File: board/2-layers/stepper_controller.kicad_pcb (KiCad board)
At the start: 4 copper layers, 99 x 46 mm, 51 parts, among them J201 USB_OTG, P103 M3_AOUT, P104 M3_BOUT, P105 M2_AOUT, P106 M2_BOUT, P107 M1_AOUT, P108 M1_BOUT, P201 UART1, P301 12V_Conn, U101 DRV8825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

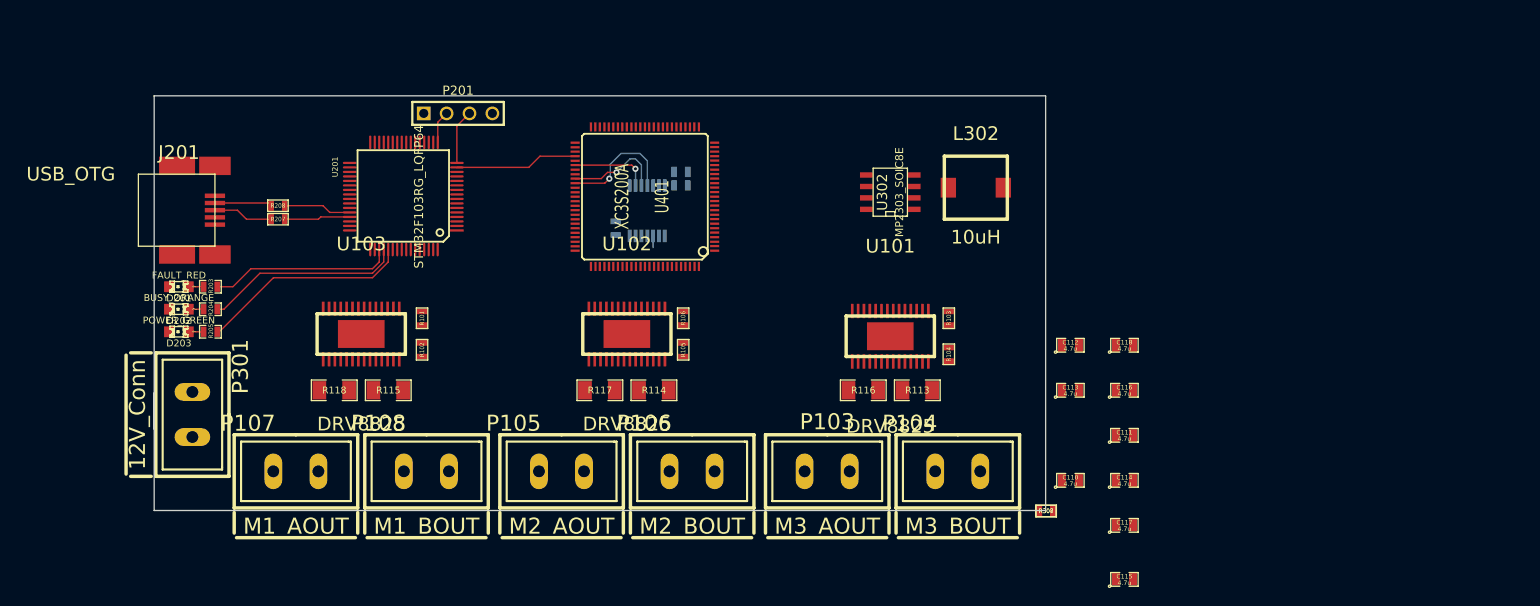
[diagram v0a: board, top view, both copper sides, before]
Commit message: routing first driver
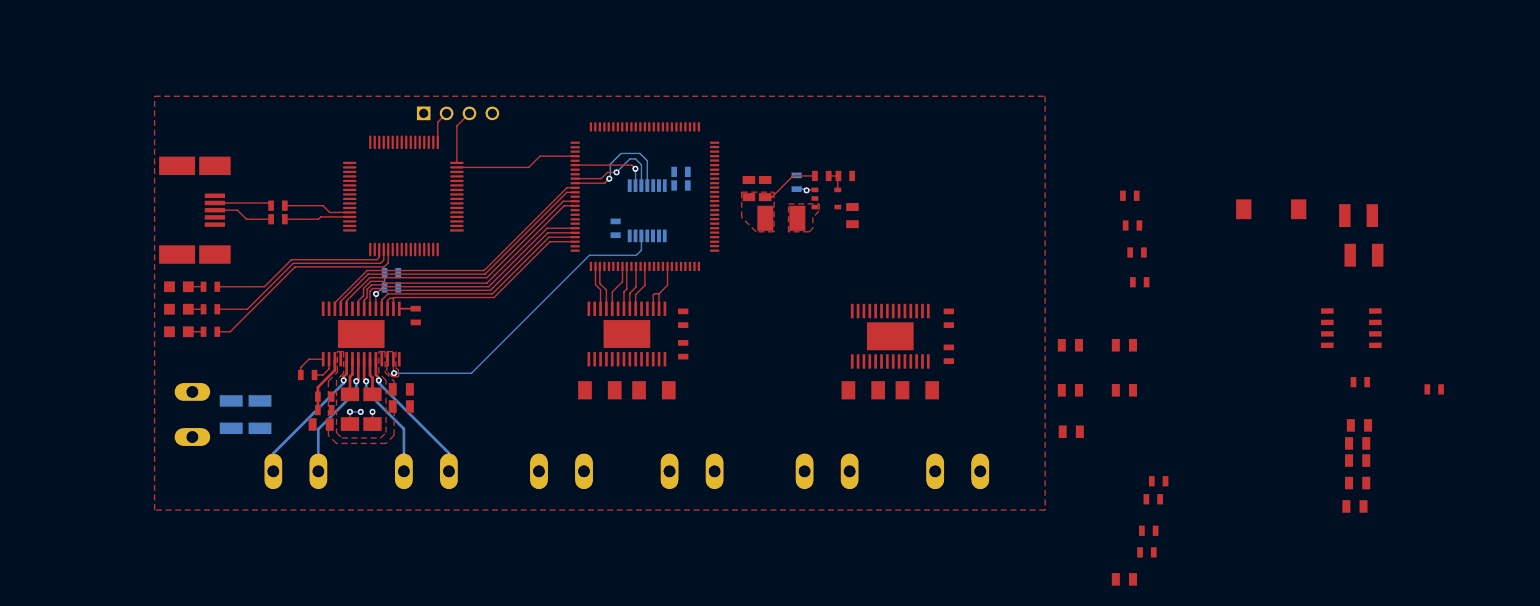
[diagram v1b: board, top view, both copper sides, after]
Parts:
- added C103: 0.47u, SM0603, F.Cu at (134.3, 110.7)
- added C106: 0.1u, SM0603, F.Cu at (124.2, 119.7)
- added C107: 10n, SM0603, F.Cu at (213.9, 100.7)
- added C108: 10n, SM0603, F.Cu at (214.4, 103.7)
- added C109: 10n, SM0603, F.Cu at (122.3, 117.3)
- added C301: 4.7u, SM0805, F.Cu at (182.8, 99.6)
- added C302: 4.7u, SM0805, F.Cu at (173.1, 96.6)
- added C303: 4.7u, SM0805, F.Cu at (171.3, 96.6)
- added C304: 10uF, SM1210, F.Cu at (239.0, 99.6)
- added C305: 10uF, SM1210, F.Cu at (239.6, 104.0)
- added C306: 4.7nF, SM0603, F.Cu at (239.2, 118.1)
- added C307: 0.1uF, SM0603, F.Cu at (215.7, 134.6)
- added C308: 10nF, SM0603, F.Cu at (215.5, 137.0)
- added C309: 1uF, SM1210, B.Cu at (117.0, 121.7)
- added C310: 4.7uF, SM1210, B.Cu at (113.8, 121.7)
- added C311: 10uF, SM0805, F.Cu at (239.1, 122.9)
- added C312: 1uF, SM0805, F.Cu at (238.9, 126.8)
- added C313: 10uF, SM0805, F.Cu at (238.9, 124.9)
- added C314: 10uF, SM0805, F.Cu at (238.9, 129.3)
- added C315: 10uF, SM0805, F.Cu at (238.6, 131.9)
- added L301: 1u, SM1210L, F.Cu at (174.9, 99.9)
- added R107: 1M, SM0603, F.Cu at (124.2, 121.2)
- added R301: 10k, SM0603, B.Cu at (176.6, 95.9)
- added R302: 200k, SM0603, F.Cu at (179.4, 95.2)
- added R303: 200k, SM0603, F.Cu at (182.0, 95.2)
- added R304: 100k, SM0603, F.Cu at (216.8, 129.1)
- added R305: 4.42k, SM0603, F.Cu at (247.4, 118.9)
- added R306: 47k, SM0603, F.Cu at (216.2, 131.1)
- added U301: MP2128-SOT23, SOT23-5, F.Cu at (179.9, 97.7)
- R101, R102: moved to B.Cu
- moved C117 89.9 mm to (123.8, 122.8), turned to 180 degrees
- moved C114 80.7 mm to (132.7, 120.8)
- moved C111 80.5 mm to (132.7, 118.9)
- moved U302 53.4 mm to (238.2, 112.1)
- moved R307 36.2 mm to (213.6, 97.4)
- moved L302 32.9 mm to (229.3, 98.9)
- moved R308 27.5 mm to (214.7, 107.0), turned to 180 degrees
- moved R102 9.15 mm to (131.6, 106.0), turned to 180 degrees
- moved C110 5.40 mm to (207.1, 123.6)
- moved R101 4.81 mm to (131.6, 107.6), turned to 0 degrees
- moved R115 2.73 mm to (129.5, 121.1), turned to 270 degrees
- moved R118 2.73 mm to (127.0, 121.1), turned to 270 degrees
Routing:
- net /VRF_0: track 0.00 -> 36.3 mm, vias 0 -> 1
- net /FPGA/M0_MODE2: track 0.00 -> 32.6 mm
- net /FPGA/M0_MODE1: track 0.00 -> 31.9 mm
- net /FPGA/M0_MODE0: track 0.00 -> 30.8 mm
- net /FPGA/M0_STEP: track 0.00 -> 30.0 mm
- net /FPGA/M0_EN: track 0.00 -> 28.4 mm
- net /FPGA/M0_DIR: track 0.00 -> 27.6 mm
- net /FPGA/M0_RESET: track 0.00 -> 25.6 mm
- net /FPGA/M0_FAULT: track 0.00 -> 25.3 mm
- net /MOT_A1_0: track 0.00 -> 15.8 mm, vias 0 -> 1
- net /MOT_B1_0: track 0.00 -> 15.8 mm, vias 0 -> 1
- net /MOT_A2_0: track 0.00 -> 14.3 mm, vias 0 -> 1
- net /MOT_B2_0: track 0.00 -> 14.3 mm, vias 0 -> 1
- net /FPGA/M1_RESET: track 0.00 -> 7.33 mm
- net +1.2V: track 0.00 -> 6.51 mm
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- added copper zone on F.Cu, net +1.2V
- added copper zone on F.Cu, net +12V
- added copper zone on F.Cu, net /VRF_0
- added copper zone on F.Cu, net GND
- added copper zone on F.Cu, net N-00000140
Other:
- board outline removed
- net class 3.3V added: clearance 0.16, trace_width 0.2, via_dia 0.6858, via_drill 0.3302

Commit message: routed 3 drivers
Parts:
- added C101: 0.47u, SM0603, F.Cu at (193.7, 109.9)
- added C102: 0.47u, SM0603, F.Cu at (163.8, 110.8)
- added C104: 0.1u, SM0603, F.Cu at (183.2, 119.7)
- added C105: 0.1u, SM0603, F.Cu at (153.7, 119.7)
- added R108: 1M, SM0603, F.Cu at (153.7, 121.2)
- added R109: 1M, SM0603, F.Cu at (183.2, 121.2)
- R103, R104, R105, R106: moved to B.Cu
- moved C108 64.1 mm to (151.8, 117.3)
- moved C110 53.8 mm to (153.3, 122.9), turned to 180 degrees
- moved C116 50.8 mm to (162.2, 120.8)
- moved C113 44.8 mm to (162.2, 118.9)
- moved C107 36.6 mm to (181.3, 117.3)
- moved R105 10.5 mm to (158.5, 105.5), turned to 0 degrees
- moved R104 9.40 mm to (188.1, 107.3), turned to 0 degrees
- moved R103 7.50 mm to (188.1, 105.8), turned to 180 degrees
- moved R106 6.80 mm to (158.5, 107.0), turned to 180 degrees
- moved R301 5.55 mm to (180.9, 99.3), turned to 90 degrees
- moved C302 4.87 mm to (177.7, 95.0), turned to 0 degrees
- moved R116 2.90 mm to (186.0, 121.1), turned to 270 degrees
- moved R101 2.89 mm to (128.8, 106.9), turned to 90 degrees
- moved R114 2.73 mm to (159.0, 121.1), turned to 270 degrees
- moved R117 2.73 mm to (156.5, 121.1), turned to 270 degrees
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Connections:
- net N-00000137 renamed /PSU/1.2_FB
- L301 pad 1: N-00000139 (its old number) -> /PSU/1.2_SW
- U101 pad 18: (no net) -> /FPGA/M2_FAULT
- U102 pad 18: (no net) -> /FPGA/M1_FAULT
- U301 pad 3: N-00000139 (its old number) -> /PSU/1.2_SW
- U401 pad 12: (no net) -> /FPGA/M2_FAULT
- U401 pad 89: (no net) -> /FPGA/M1_FAULT
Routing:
- net /VRF_2: track 0.00 -> 47.1 mm, vias 0 -> 1
- net /FPGA/M2_RESET: track 0.00 -> 31.5 mm
- net /FPGA/M2_FAULT: track 0.00 -> 28.8 mm
- net /FPGA/M2_DIR: track 0.00 -> 27.2 mm
- net /FPGA/M2_EN: track 0.00 -> 26.3 mm
- net /FPGA/M2_STEP: track 0.00 -> 24.4 mm
- net /FPGA/M2_MODE0: track 0.00 -> 22.9 mm
- net /FPGA/M2_MODE1: track 0.00 -> 22.0 mm
- net /FPGA/M2_MODE2: track 0.00 -> 21.1 mm
- net /VRF_1: track 0.00 -> 17.8 mm, vias 0 -> 1
- net /MOT_A1_2: track 0.00 -> 15.8 mm, vias 0 -> 1
- net /MOT_A1_1: track 0.00 -> 15.8 mm, vias 0 -> 1
- net /MOT_B1_2: track 0.00 -> 15.8 mm, vias 0 -> 1
- net /MOT_B1_1: track 0.00 -> 15.8 mm, vias 0 -> 1
- net /MOT_A2_2: track 0.00 -> 14.3 mm, vias 0 -> 1
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- added copper zone on F.Cu, net /VRF_1
- added copper zone on F.Cu, net /VRF_2
- removed copper zone on F.Cu, net N-00000140 (its old number)
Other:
- net class 12V: via_dia 0.6858 -> 0.6096; via_drill 0.3302 -> 0.3
- net class 3.3V: via_dia 0.6858 -> 0.6096; via_drill 0.3302 -> 0.3
- net class Default: via_dia 0.6858 -> 0.6096; via_drill 0.3302 -> 0.3
- net class current sense: via_dia 0.6858 -> 0.6096; via_drill 0.3302 -> 0.3

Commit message: RER B blablabla
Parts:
- added C208: CSMALL, SM0603, F.Cu at (143.2, 101.9)
- added C209: CSMALL, SM0603, F.Cu at (143.7, 91.8)
- added X201: TXC_50X32_AB, XTAL_5.0x3.2mm, F.Cu at (143.7, 97.4)
- moved P201 7.83 mm to (135.5, 81.2)
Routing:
- net /STM32//CLR_DAC: track 0.00 -> 24.4 mm, vias 0 -> 1
- net /STM32/FPGA_INITB: track 0.00 -> 22.6 mm
- net /FPGA/DIN: track 0.00 -> 20.8 mm, vias 0 -> 2
- net /FPGA/CCLK: track 0.00 -> 19.2 mm
- net N-0000090: track 6.08 -> 0.00 mm
- net N-0000091: track 3.62 -> 0.00 mm
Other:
- board outline added: 99 x 46 mm

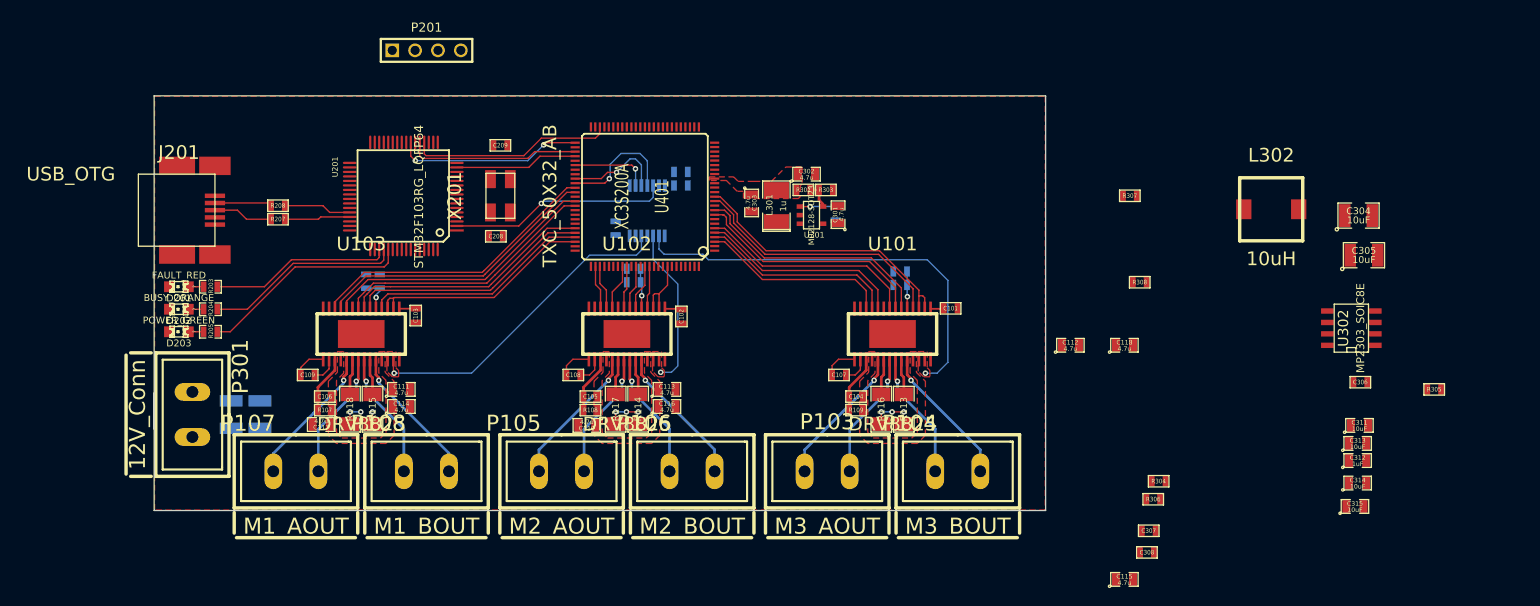
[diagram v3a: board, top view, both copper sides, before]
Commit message: routed 12->3.3v miss mezzanine header
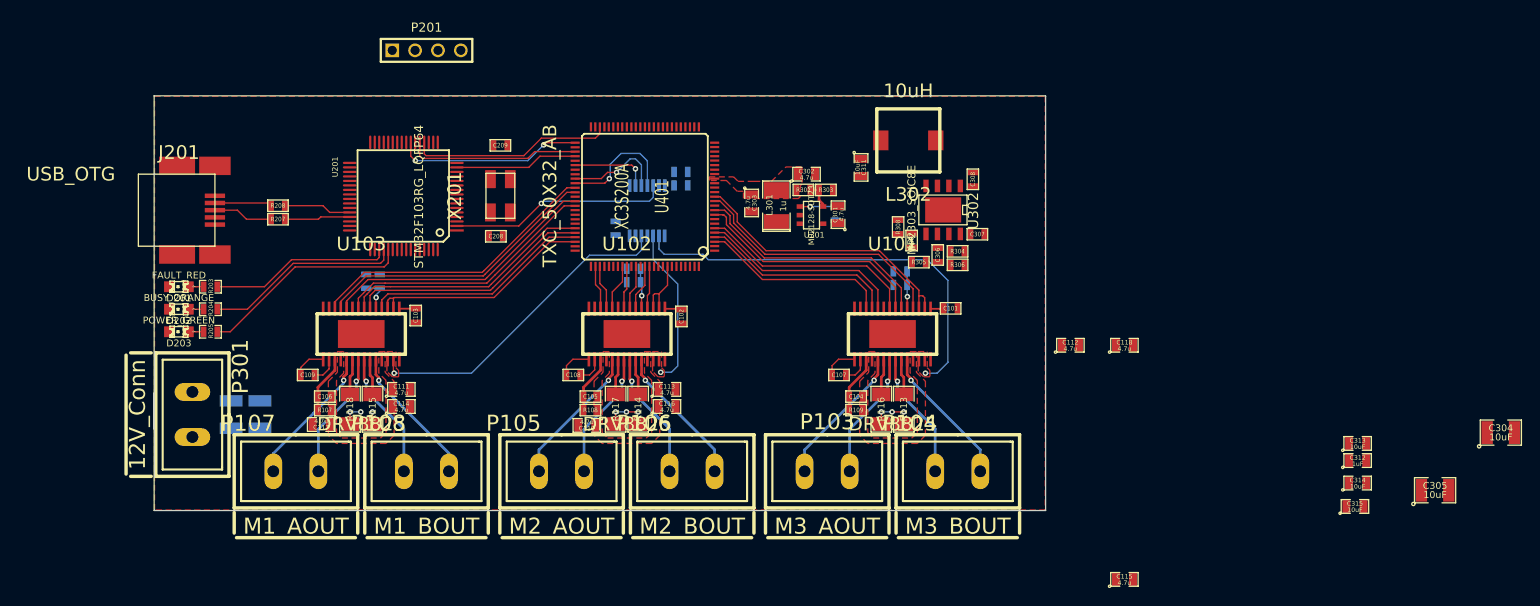
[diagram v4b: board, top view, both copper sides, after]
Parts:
- U302: footprint SO8E -> SO8_WITH_EP
- moved C311 62.3 mm to (183.8, 94.2), turned to 270 degrees
- moved R305 58.9 mm to (190.2, 104.8), turned to 180 degrees
- moved C306 49.0 mm to (192.3, 104.0), turned to 270 degrees
- moved U302 47.2 mm to (192.9, 99.0), turned to 180 degrees
- moved C308 45.7 mm to (196.2, 95.6), turned to 90 degrees
- moved L302 41.0 mm to (189.0, 91.2), turned to 180 degrees
- moved C307 38.0 mm to (196.7, 101.7)
- moved R304 33.9 mm to (194.5, 103.6), turned to 180 degrees
- moved R306 33.9 mm to (194.5, 105.1)
- moved C304 28.8 mm to (254.8, 123.7)
- moved R308 27.5 mm to (187.9, 100.9), turned to 90 degrees
- moved C305 27.3 mm to (247.5, 130.1)
- moved R307 24.7 mm to (189.4, 102.4), turned to 90 degrees

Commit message: blabla vroum vroum
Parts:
- added C201: 1uF, SM0603, F.Cu at (209.7, 126.3)
- added C202: 1uF, SM0603, F.Cu at (213.2, 127.7)
- added C203: 1uF, SM0603, F.Cu at (209.7, 129.0)
- added C204: 1uF, SM0603, F.Cu at (209.7, 131.0)
- added C205: 1uF, SM0603, F.Cu at (209.7, 132.6)
- added C206: 1uF, SM0603, F.Cu at (209.7, 134.2)
- added C207: 1uF, SM0603, F.Cu at (209.7, 136.6)
- added C408: 1u, SM0603, F.Cu at (157.0, 88.0)
- added C409: 100n, SM0603, F.Cu at (167.9, 89.5)
- added C410: 1u, SM0603, B.Cu at (154.0, 99.5)
- added C411: 100n, SM0603, B.Cu at (150.4, 101.2)
- added C412: 1u, SM0603, B.Cu at (153.6, 106.8)
- added C413: 100n, SM0603, F.Cu at (164.5, 107.3)
- added C414: 1u, SM0603, B.Cu at (166.6, 97.9)
- added C415: 100n, SM0603, B.Cu at (166.6, 99.5)
- added R201: 0, SM0603, B.Cu at (125.2, 100.6)
- added R202: 10k, SM0603, B.Cu at (127.7, 100.6)
- added R206: 1.5k, SM0603, B.Cu at (121.4, 97.9)
- added R209: 10k, SM0603, B.Cu at (122.6, 93.6)
- added R210: 0, SM0603, B.Cu at (125.2, 93.6)
- moved C208 8.35 mm to (134.9, 101.0), turned to 0 degrees
- moved X201 8.00 mm to (135.8, 98.2), turned to 0 degrees
- moved U201 7.77 mm to (125.2, 97.0)
- moved C209 6.35 mm to (140.2, 97.1)
- moved R207 3.54 mm to (115.5, 99.5)
- moved R208 3.54 mm to (115.5, 98.0)
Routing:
- net /STM32//CLR_DAC: track 24.4 -> 0.00 mm, vias 1 -> 0
- net N-0000095: track 23.6 -> 0.00 mm
- net /STM32/FPGA_INITB: track 22.6 -> 0.00 mm
- net N-0000097: track 21.9 -> 0.00 mm
- net /FPGA/DIN: track 20.8 -> 0.00 mm, vias 2 -> 0
- net N-0000099: track 20.2 -> 0.00 mm
- net /FPGA/CCLK: track 19.2 -> 0.00 mm
- net /FPGA/DONE: track 13.6 -> 0.00 mm
- net D-: track 7.52 -> 0.00 mm
- net D+: track 7.31 -> 0.00 mm
- net N-00000126: track 6.65 -> 0.00 mm
- net N-00000125: track 6.36 -> 0.00 mm
- net /FPGA/M2_RESET: track 31.5 -> 32.1 mm
